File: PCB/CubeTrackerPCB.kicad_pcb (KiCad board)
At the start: 2 copper layers, 28 x 50.9 mm, 9 parts, among them U1 XIAO-RP2040-DIP, U2 ICM-42688-P, U3 DM-OLED096-636

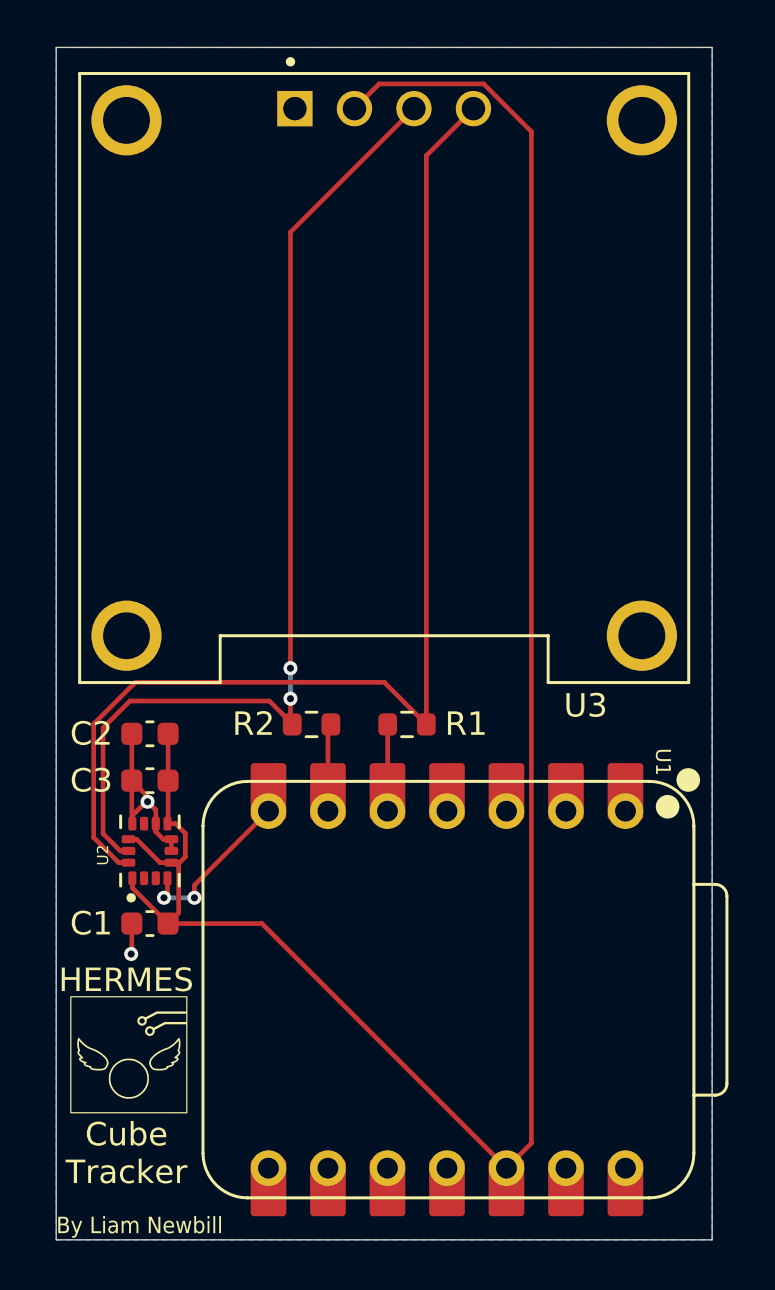
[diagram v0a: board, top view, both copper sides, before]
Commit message: updated pullup resistors
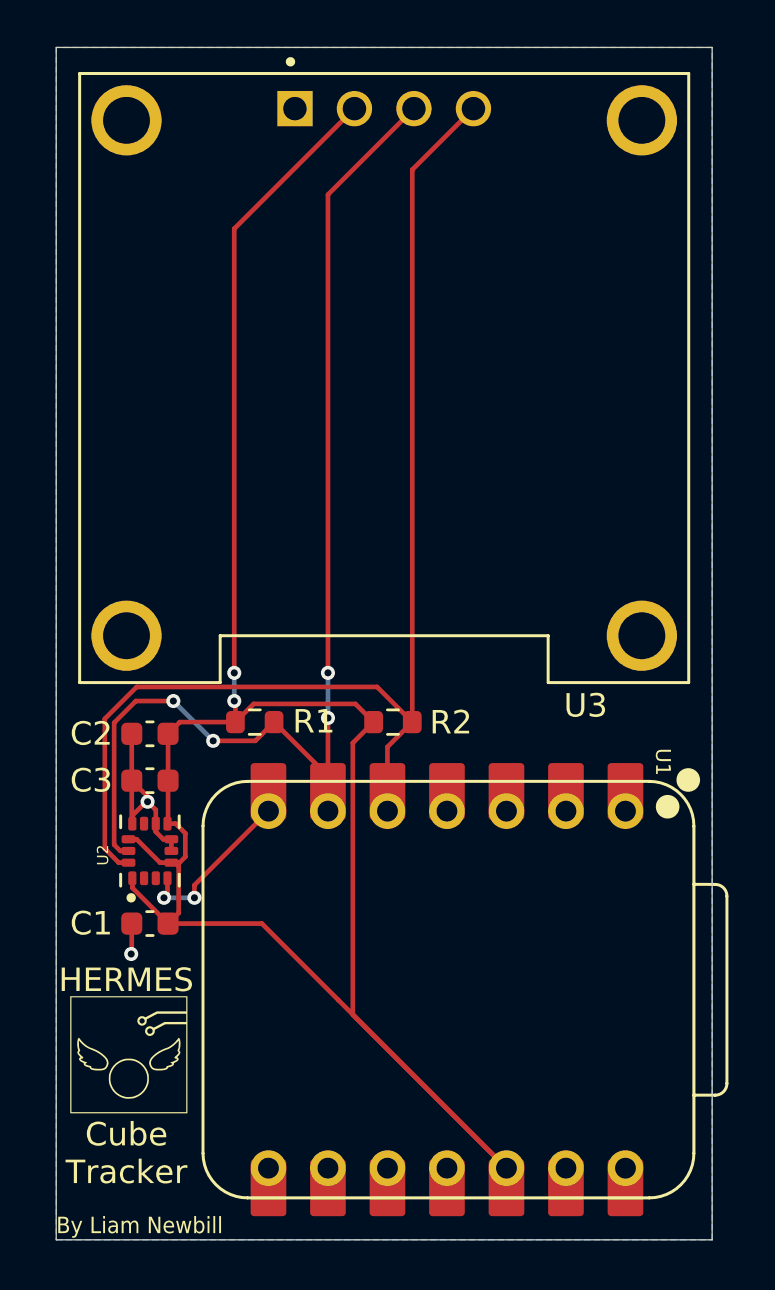
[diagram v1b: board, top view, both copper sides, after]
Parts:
- moved R1 6.50 mm to (156.5, 77.7)
- moved R2 3.48 mm to (162.4, 77.7), turned to 0 degrees
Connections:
- R1 pad 1: SDA -> SCL
- R1 pad 2: Net-(U1-GPIO6/SDA) -> 3.3V
- R2 pad 1: Net-(U1-GPIO7/SCL) -> 3.3V
- R2 pad 2: SCL -> SDA
- U1 pad 5: Net-(U1-GPIO6/SDA) -> SDA
- U1 pad 6: Net-(U1-GPIO7/SCL) -> SCL
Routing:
- net SCL: track 43.1 -> 50.4 mm, vias 2 -> 4
- net 3.3V: track 86.4 -> 93.0 mm, vias 0 -> 2
- net Net-(U1-GPIO6/SDA): track 3.69 -> 0.00 mm
- net Net-(U1-GPIO7/SCL): track 3.58 -> 0.00 mm
- net SDA: track 49.6 -> 52.6 mm

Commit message: Changed Layout
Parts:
- U1: moved to B.Cu
- moved U1 26.1 mm to (162.1, 63.1), turned to 0 degrees
- moved C1 22.0 mm to (162.2, 66.8)
- moved C2 22.0 mm to (162.2, 58.7)
- moved C3 22.0 mm to (162.2, 60.7)
- moved U2 22.0 mm to (162.2, 63.7)
- moved G*** 21.9 mm to (158.1, 71.1)
- moved R1 19.4 mm to (157.5, 58.3), turned to 0 degrees
- moved R2 17.5 mm to (157.5, 60.9), turned to 180 degrees
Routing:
- net 3.3V: track 93.0 -> 46.9 mm, vias 2 -> 0
- net SDA: track 52.6 -> 22.7 mm, vias 0 -> 2
- net SCL: track 50.4 -> 23.2 mm, vias 4 -> 0
- net ICMINT: track 7.21 -> 18.2 mm
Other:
- board size 28 x 50.9 mm -> 26.6 x 26.6 mm
